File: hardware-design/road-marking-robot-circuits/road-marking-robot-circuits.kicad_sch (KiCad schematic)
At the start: 26 parts, among them IC1 ATMEGA2560-A, J1 Barrel_Jack, J2 u-sonic-1, Q1 PMOS, SW1 SW_SPST, U1 LM7909_TO220, U2 LM7812_TO220, U3 LM7805_TO220, U4 LM7806_TO220

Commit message: [ADDS] solenoid valve relay
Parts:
- removed IC1: ATMEGA2560-A, TQFP100, symbol core-cache:ATMEGA2560-A
- added A1: Arduino_Mega2560_R3_Shield, PCM_arduino-library:Arduino_Mega2560_R3_Shield, symbol PCM_arduino-library:Arduino_Mega2560_R3_Shield
- added D3: 1N4001, Diode_THT:D_DO-41_SOD81_P10.16mm_Horizontal, symbol Diode:1N4001
- added J3: u-sonic-2, symbol Connector:Conn_01x04_Pin
- added J4: u-sonic-3, symbol Connector:Conn_01x04_Pin
- added J5: u-sonic-4, symbol Connector:Conn_01x04_Pin
- added J6: u-sonic-5, symbol Connector:Conn_01x04_Pin
- added J7: FLOW_METER, symbol Connector:Conn_01x03_Pin
- added J8: 12V solenoid, symbol Connector:Conn_01x02_Pin
- added K1: FINDER-36.11, Relay_THT:Relay_SPDT_Finder_36.11, symbol Relay:FINDER-36.11
- added Q2: BC547, Package_TO_SOT_THT:TO-92_Inline, symbol Transistor_BJT:BC547
- added U5: ~, symbol my-modules:NEO-6M-GPS-MODULE
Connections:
- net 12V_REG: now also A1.VIN
- net 5V_REG: now also A2.1 (VCC), D3.1 (K), J3.4 (Pin_4), J4.4 (Pin_4), J5.4 (Pin_4), J6.4 (Pin_4), J7.3 (Pin_3), K1.A2, U5.1 (VCC)
- net Earth: now also A1.GND6 (GND), J3.1 (Pin_1), J4.1 (Pin_1), J5.1 (Pin_1), J6.1 (Pin_1), J7.1 (Pin_1), Q2.3 (E), U5.4 (GND)
- net US1_EC: now reaches J2.2 (Pin_2)
- net US1_EC: now also A1.D35
- net US1_TR: now reaches J2.3 (Pin_3)
- net US1_TR: now also A1.D30
- net MPU_SCL: now reaches A2.3 (SCL)
- net MPU_SCL: now also A1.D21 (D21/SCL)
- net MPU_SDA: now reaches A2.4 (SDA)
- net MPU_SDA: now also A1.D20 (D20/SDA)
- new net: J8.1 (Pin_1), K1.11
- new net: J8.2 (Pin_2), K1.14
- new net: D3.2 (A), K1.A1, Q2.1 (C)
- new net FLOW_METER: A1.D10, J7.2 (Pin_2)
- new net GPS_RX: A1.D18 (D18/TX1), U5.2 (RX)
- new net GPS_TX: A1.D19 (D19/RX1), U5.3 (TX)
- new net SOLND_REL: A1.A15, Q2.2 (B)
- new net US2_EC: A1.D36, J3.2 (Pin_2)
- new net US2_TR: A1.D31, J3.3 (Pin_3)
- new net US3_EC: A1.D37, J4.2 (Pin_2)
- new net US3_TR: A1.D32, J4.3 (Pin_3)
- new net US4_EC: A1.D38, J5.2 (Pin_2)
- new net US4_TR: A1.D33, J5.3 (Pin_3)
- new net US5_EC: A1.D39, J6.2 (Pin_2)
- new net US5_TR: A1.D34, J6.3 (Pin_3)
- no-connect marks 0 -> 10
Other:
- note added: "1/2" Diameter F=7.5*Q(L/min)"
- note added: "NDP6020P-PX"
- note added: "NO to prevent leakage on boot"
- moved on the sheet: A2, HS1, HS2, HS3, HS4, J2

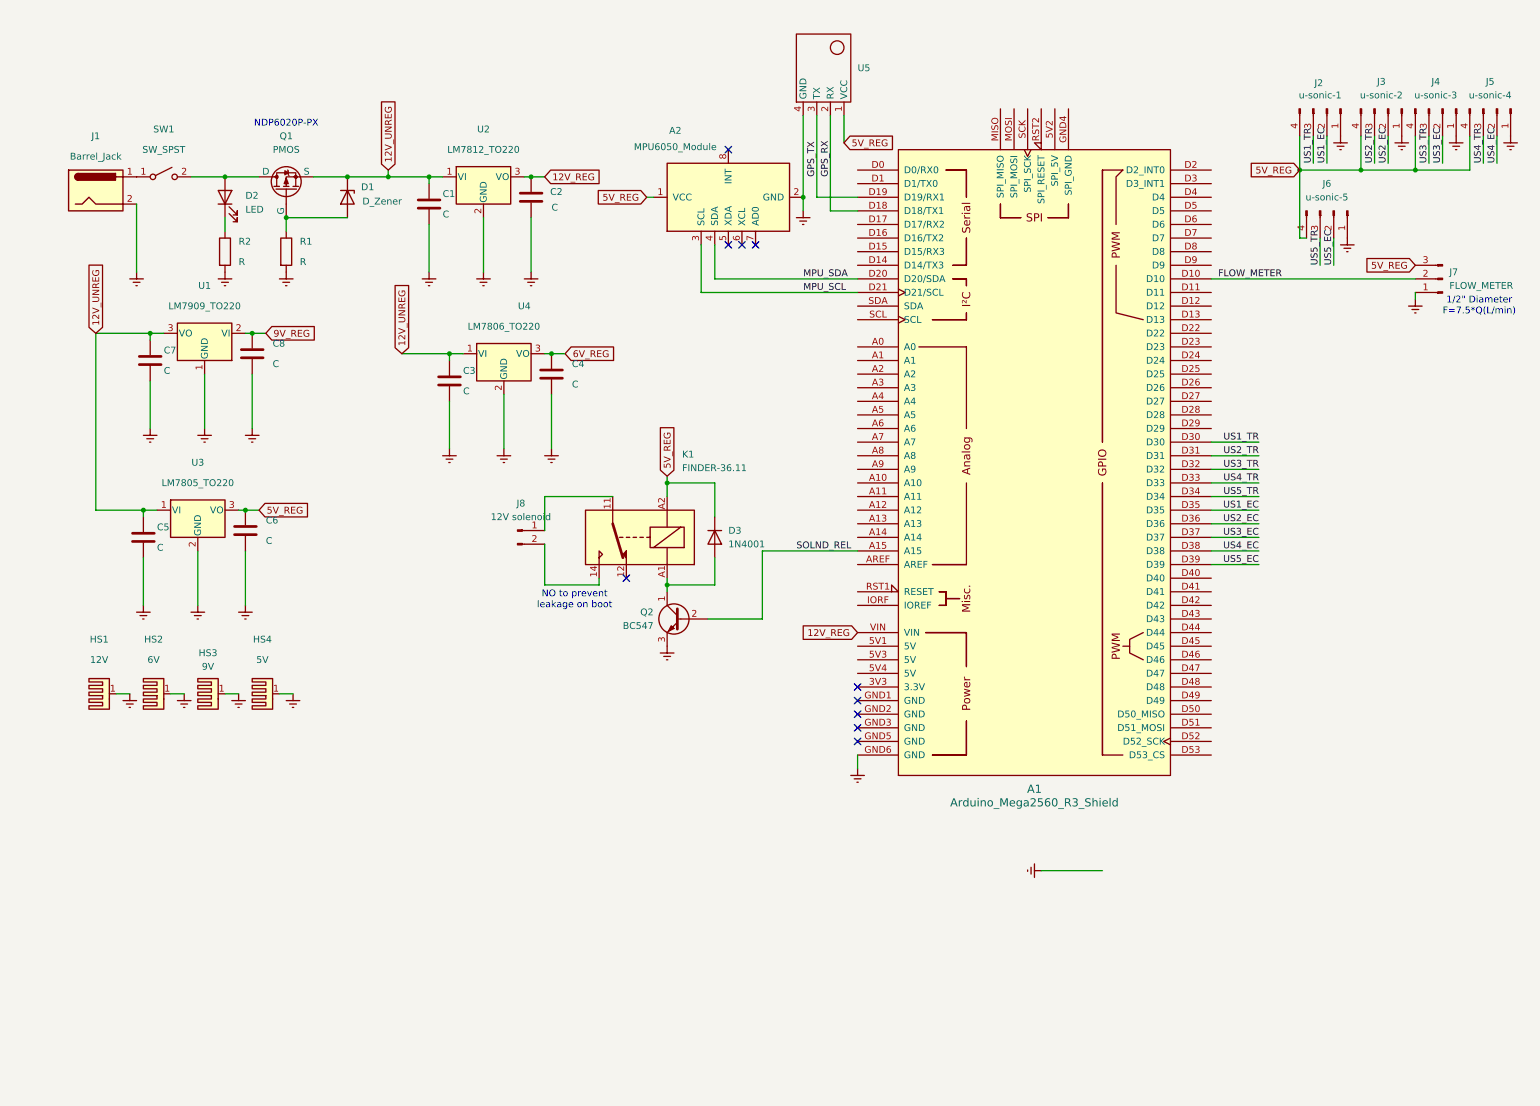
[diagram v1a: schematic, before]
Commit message: adds footprints
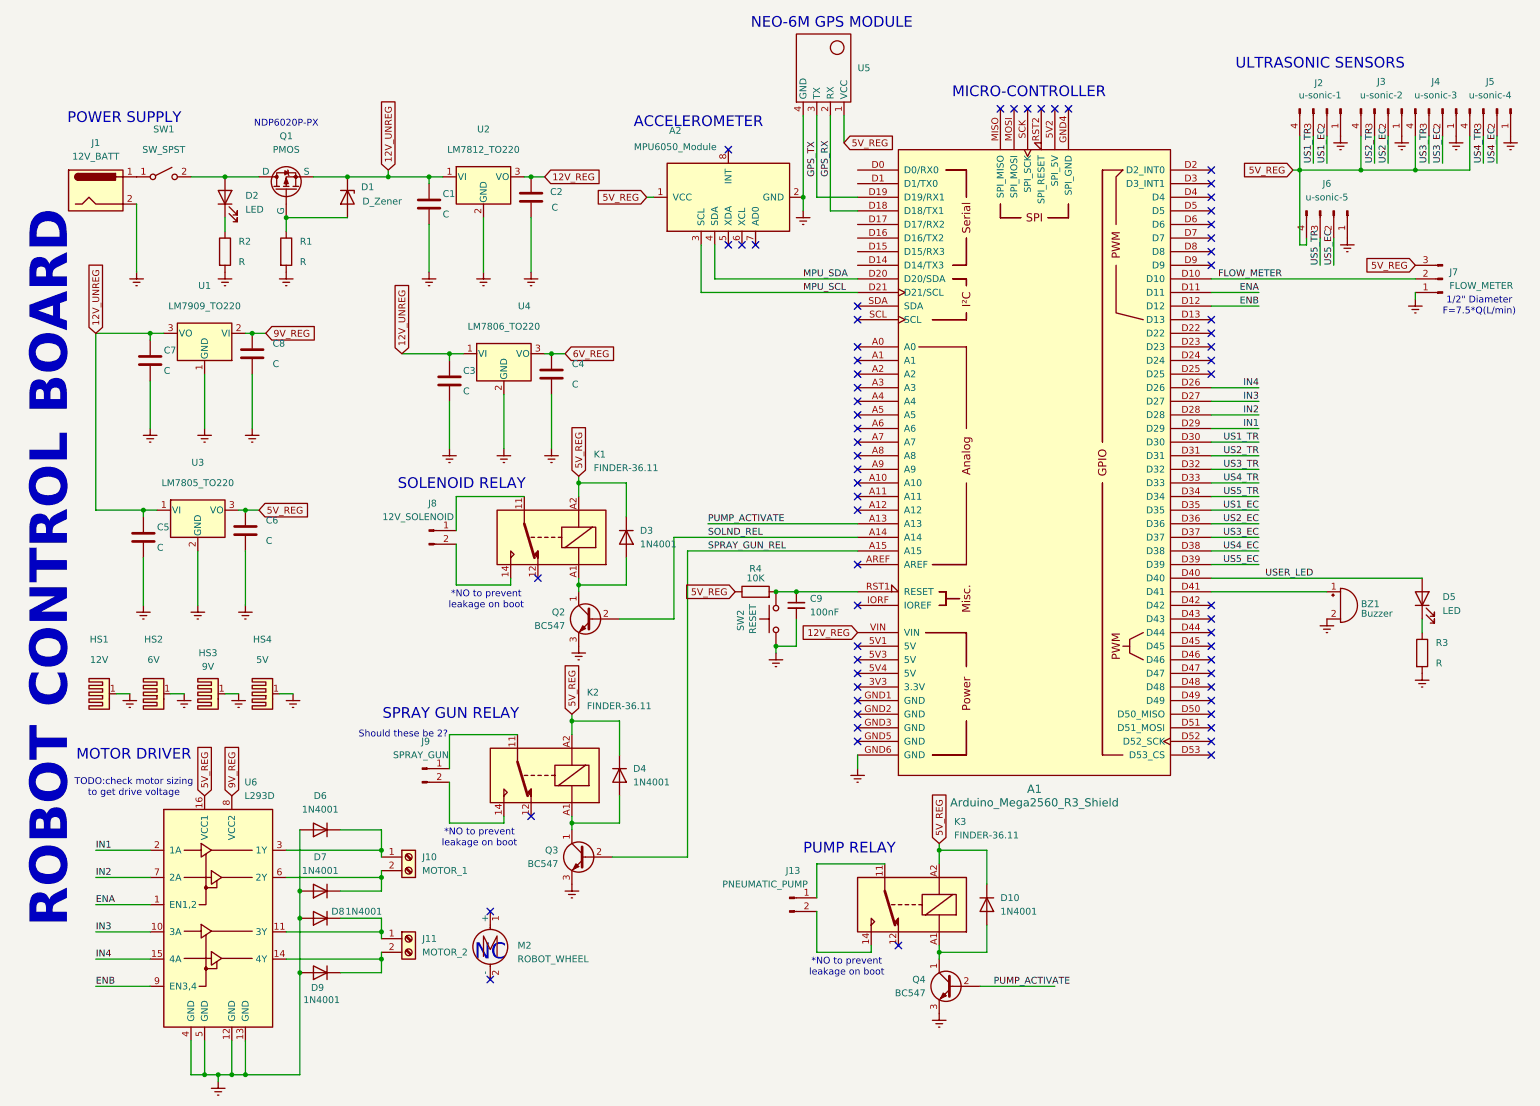
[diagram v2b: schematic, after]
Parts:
- added BZ1: Buzzer, Buzzer_Beeper:Buzzer_12x9.5RM7.6, symbol Device:Buzzer
- added C9: 100nF, Capacitor_THT:CP_Radial_D4.0mm_P2.00mm, symbol Device:C_Small
- added D10, D4, D6, D7, D8, D9: 1N4001, Diode_THT:D_DO-41_SOD81_P10.16mm_Horizontal, symbol Diode:1N4001
- added D5: LED, LED_THT:LED_D3.0mm, symbol Device:LED
- added J10: MOTOR_1, TerminalBlock:TerminalBlock_bornier-2_P5.08mm, symbol Connector:Screw_Terminal_01x02
- added J11: MOTOR_2, TerminalBlock:TerminalBlock_bornier-2_P5.08mm, symbol Connector:Screw_Terminal_01x02
- added J13: PNEUMATIC_PUMP, Connector_PinHeader_2.54mm:PinHeader_1x02_P2.54mm_Vertical, symbol Connector:Conn_01x02_Pin
- added J9: SPRAY_GUN, Connector_PinHeader_2.54mm:PinHeader_1x02_P2.54mm_Vertical, symbol Connector:Conn_01x02_Pin
- added K2, K3: FINDER-36.11, Relay_THT:Relay_SPDT_Finder_36.11, symbol Relay:FINDER-36.11
- added M2: ROBOT_WHEEL, symbol Motor:Motor_DC
- added Q3, Q4: BC547, Package_TO_SOT_THT:TO-92_Inline, symbol Transistor_BJT:BC547
- added R3: R, Resistor_THT:R_Axial_DIN0309_L9.0mm_D3.2mm_P20.32mm_Horizontal, symbol Device:R
- added R4: 10K, Resistor_THT:R_Axial_DIN0309_L9.0mm_D3.2mm_P20.32mm_Horizontal, symbol Device:R
- added SW2: RESET, Button_Switch_THT:SW_Tactile_Straight_KSA0Axx1LFTR, symbol Switch:SW_Push
- added U6: L293D, Package_DIP:DIP-16_W7.62mm, symbol Driver_Motor:L293D
- C1, C2, C3, C4, C5, C6, C7, C8: footprint (none) -> Capacitor_THT:CP_Radial_D4.0mm_P2.00mm
- D1: footprint (none) -> Diode_THT:D_DO-15_P12.70mm_Horizontal
- D2: footprint (none) -> LED_THT:LED_D3.0mm
- HS1, HS2, HS3, HS4: footprint (none) -> Heatsink:Heatsink_Stonecold_HS-S02_13.21x9.53mm
- J1: value Barrel_Jack -> 12V_BATT; footprint (none) -> Connector_BarrelJack:BarrelJack_Horizontal
- J2, J3, J4, J5, J6: footprint (none) -> Connector_PinHeader_2.54mm:PinHeader_1x04_P2.54mm_Vertical
- J7, SW1: footprint (none) -> Connector_PinHeader_2.54mm:PinHeader_1x02_P2.54mm_Vertical
- J8: value 12V solenoid -> 12V_SOLENOID; footprint (none) -> Connector_PinHeader_2.54mm:PinHeader_1x02_P2.54mm_Vertical
- Q1: footprint (none) -> Package_TO_SOT_THT:TO-220-3_Vertical
- R1, R2: footprint (none) -> Resistor_THT:R_Axial_DIN0309_L9.0mm_D3.2mm_P20.32mm_Horizontal
- U5: footprint (none) -> my-modules:NEO-6M-GPS-MODULE
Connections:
- net 5V_REG: now also D10.1 (K), D4.1 (K), K2.A2, K3.A2, R4.1, U6.16 (VCC1)
- net 9V_REG: now also U6.8 (VCC2)
- net Earth: now also BZ1.2 (-), C9.2, D6.2 (A), D7.2 (A), D8.2 (A), D9.2 (A), Q3.3 (E), Q4.3 (E), R3.2, SW2.1, U6.12 (GND), U6.13 (GND), U6.4 (GND), U6.5 (GND)
- net SOLND_REL: now also A1.A14; no longer A1.A15
- net PUMP_ACTIVATE: now reaches A1.A13
- net PUMP_ACTIVATE: now also Q4.2 (B)
- net ENA: now reaches A1.D11
- net ENA: now also U6.1 (EN1,2)
- net ENB: now reaches A1.D12
- net ENB: now also U6.9 (EN3,4)
- net IN4: now reaches A1.D26
- net IN4: now also U6.15 (4A)
- net IN3: now reaches A1.D27
- net IN3: now also U6.10 (3A)
- net IN2: now reaches A1.D28
- net IN2: now also U6.7 (2A)
- net IN1: now reaches A1.D29
- net IN1: now also U6.2 (1A)
- net USER_LED: now reaches A1.D40
- net USER_LED: now also D5.2 (A)
- net at A1.D41: now also BZ1.1 (+)
- net at A1.RST1 (RESET): now also C9.1, R4.2, SW2.2
- new net: J9.1 (Pin_1), K2.11
- new net: J9.2 (Pin_2), K2.14
- new net: D10.2 (A), K3.A1, Q4.1 (C)
- new net: J13.1 (Pin_1), K3.11
- new net: J13.2 (Pin_2), K3.14
- new net: D6.1 (K), J10.1 (Pin_1), U6.3 (1Y)
- new net: D7.1 (K), J10.2 (Pin_2), U6.6 (2Y)
- new net: D4.2 (A), K2.A1, Q3.1 (C)
- new net: D8.1 (K), J11.1 (Pin_1), U6.11 (3Y)
- new net: D9.1 (K), J11.2 (Pin_2), U6.14 (4Y)
- new net: D5.1 (K), R3.1
- new net SPRAY_GUN_REL: A1.A15, Q3.2 (B)
- no-connect marks 10 -> 65
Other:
- note added: "*NO to prevent leakage on boot"
- note added: "ACCELEROMETER"
- note added: "MICRO-CONTROLLER"
- note added: "MOTOR DRIVER"
- note added: "NC"
- note added: "NEO-6M GPS MODULE"
- note added: "POWER SUPPLY"
- note added: "PUMP RELAY"
- note added: "ROBOT CONTROL BOARD"
- note added: "SOLENOID RELAY"
- note added: "SPRAY GUN RELAY"
- note added: "Should these be 2?"
- note added: "TODO:check motor sizing to get drive voltage"
- note added: "ULTRASONIC SENSORS"
- note removed: "NO to prevent leakage on boot"
- moved on the sheet: D3, J8, K1, Q2

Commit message: [UPDATES] arduino position
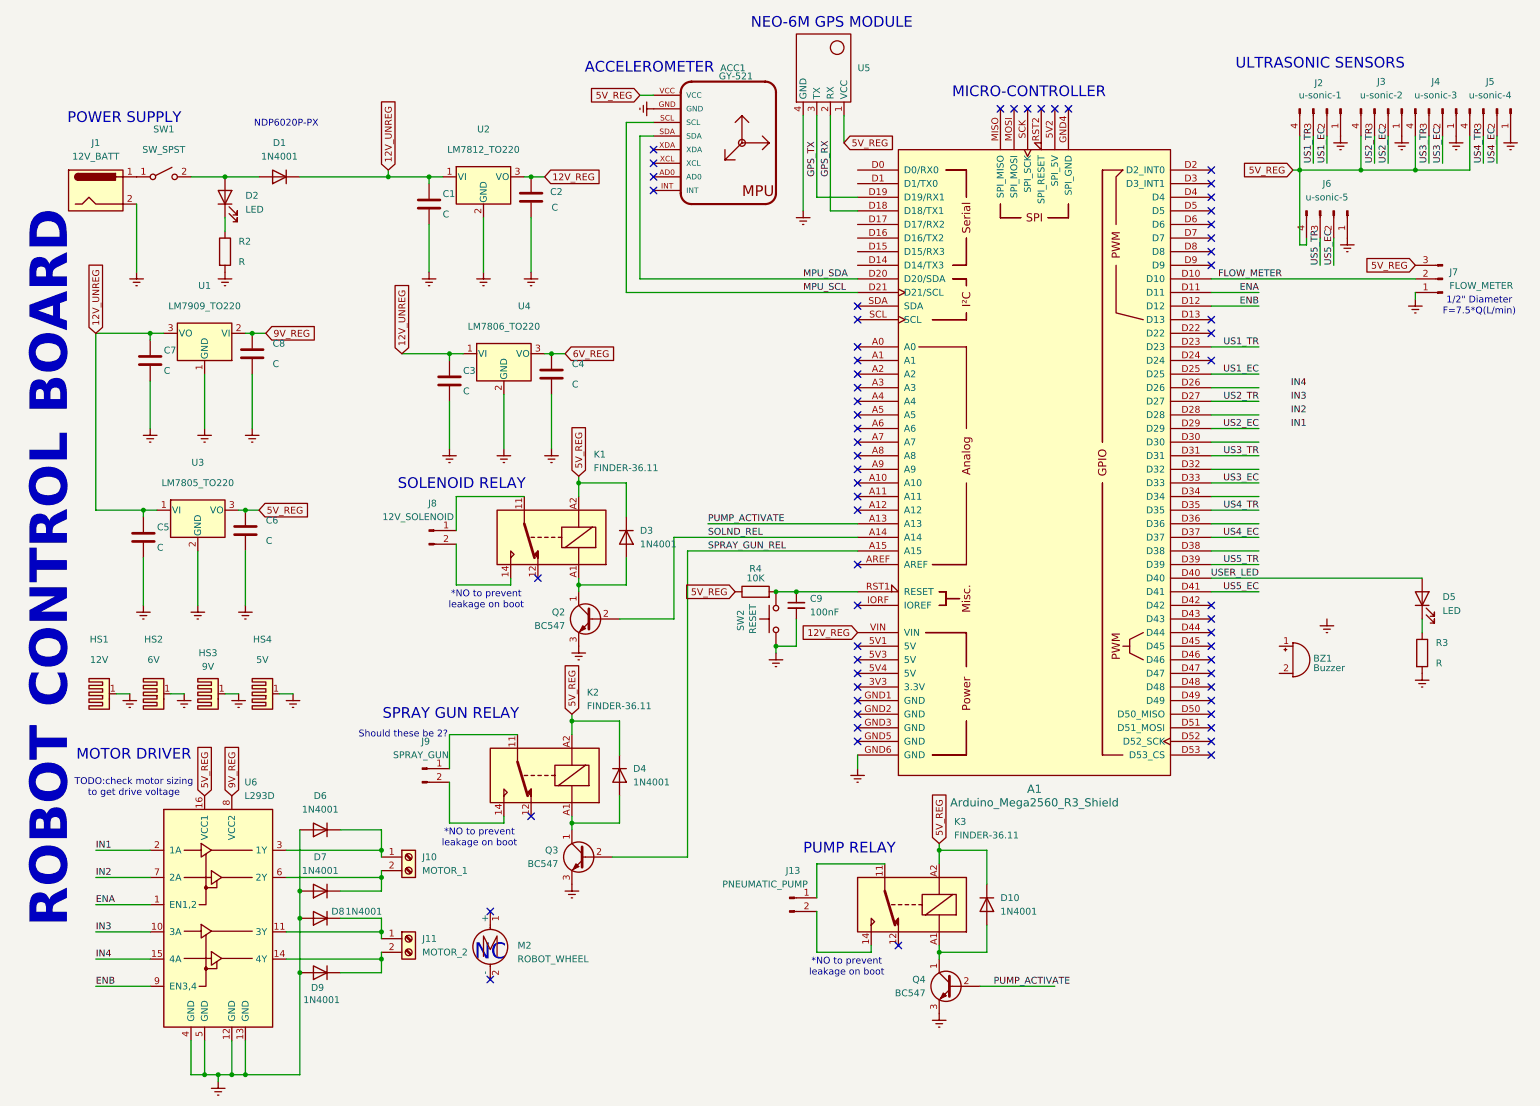
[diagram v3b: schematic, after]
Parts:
- removed A2: MPU6050_Module, Charleslabs_Parts:MPU6050_Module, symbol Charleslabs_Parts:MPU6050_Module
- removed D1: D_Zener, Diode_THT:D_DO-15_P12.70mm_Horizontal, symbol Device:D_Zener
- removed Q1: PMOS, Package_TO_SOT_THT:TO-220-3_Vertical, symbol Simulation_SPICE:PMOS
- removed R1: R, Resistor_THT:R_Axial_DIN0309_L9.0mm_D3.2mm_P20.32mm_Horizontal, symbol Device:R
- added ACC1: GY-521, MPU6050-MODULE:GY-521, symbol GY-521:GY-521
- added D1: 1N4001, Diode_THT:D_DO-41_SOD81_P10.16mm_Horizontal, symbol Diode:1N4001
- J7: footprint Connector_PinHeader_2.54mm:PinHeader_1x02_P2.54mm_Vertical -> Connector_PinHeader_2.54mm:PinHeader_1x03_P2.54mm_Vertical
- R2, R3, R4: footprint Resistor_THT:R_Axial_DIN0309_L9.0mm_D3.2mm_P20.32mm_Horizontal -> Resistor_THT:R_Axial_DIN0309_L9.0mm_D3.2mm_P12.70mm_Horizontal
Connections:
- net 12V_UNREG: now also D1.1 (K)
- net 5V_REG: now also ACC1.VCC
- net Earth: now also ACC1.GND; no longer BZ1.2 (-)
- net IN1: no longer A1.D29
- net IN2: no longer A1.D28
- net IN3: no longer A1.D27
- net IN4: no longer A1.D26
- net MPU_SCL: now also ACC1.SCL
- net MPU_SDA: now also ACC1.SDA
- net US1_EC: now also A1.D25; no longer A1.D35
- net US1_TR: now also A1.D23; no longer A1.D30
- net US2_EC: now also A1.D29; no longer A1.D36
- net US2_TR: now also A1.D27; no longer A1.D31
- net US3_EC: now also A1.D33; no longer A1.D37
- net US3_TR: now also A1.D31; no longer A1.D32
- net US4_EC: now also A1.D37; no longer A1.D38
- net US4_TR: now also A1.D35; no longer A1.D33
- net US5_EC: now also A1.D41; no longer A1.D39
- net US5_TR: now also A1.D39; no longer A1.D34
- net at D2.2 (A), SW1.2 (B): now also D1.2 (A)
- net at BZ1.1 (+): no longer A1.D41
- no-connect marks 65 -> 63
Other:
- moved on the sheet: BZ1

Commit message: [UPDATES] PCB design
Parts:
- added D11, D12, D13: ACTIVE?, LED_THT:LED_D3.0mm, symbol Device:LED
- added H1, H2, H3, H4: MountingHole, MountingHole:MountingHole_3.2mm_M3, symbol Mechanical:MountingHole
- added R1, R5, R6: R, Resistor_THT:R_Axial_DIN0309_L9.0mm_D3.2mm_P12.70mm_Horizontal, symbol Device:R
- J13, J8, J9: footprint Connector_PinHeader_2.54mm:PinHeader_1x02_P2.54mm_Vertical -> TerminalBlock:TerminalBlock_bornier-2_P5.08mm
- J7: footprint Connector_PinHeader_2.54mm:PinHeader_1x03_P2.54mm_Vertical -> TerminalBlock:TerminalBlock_bornier-3_P5.08mm
- Q2, Q3, Q4: footprint Package_TO_SOT_THT:TO-92_Inline -> Package_TO_SOT_THT:TO-92_Inline_Wide
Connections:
- net 5V_REG: now also D11.2 (A), D12.2 (A), D13.2 (A)
- net IN1: now also A1.D14 (D14/TX3)
- net IN2: now also A1.D15 (D15/RX3)
- net IN3: now also A1.D16 (D16/TX2)
- net IN4: now also A1.D17 (D17/RX2)
- net at D10.2 (A), K3.A1, Q4.1 (C): now also R1.2
- net at D3.2 (A), K1.A1, Q2.1 (C): now also R5.2
- net at D4.2 (A), K2.A1, Q3.1 (C): now also R6.2
- new net: D12.1 (K), R5.1
- new net: D13.1 (K), R6.1
- new net: D11.1 (K), R1.1
